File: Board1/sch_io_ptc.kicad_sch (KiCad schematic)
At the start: 5 parts, among them J2 PTC Plate, Q1 2N7002E, U4 AQG22205

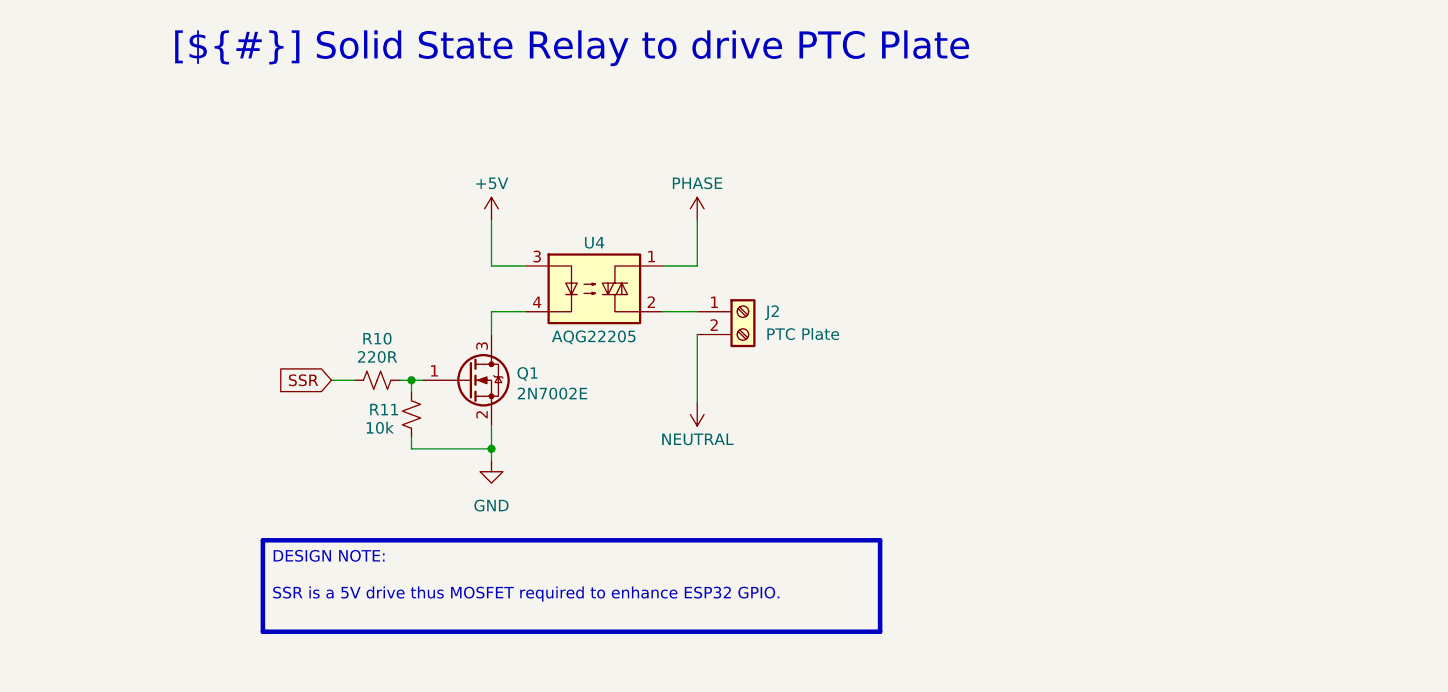
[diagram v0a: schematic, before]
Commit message: Resolve library and ERC issues
No changes to design.
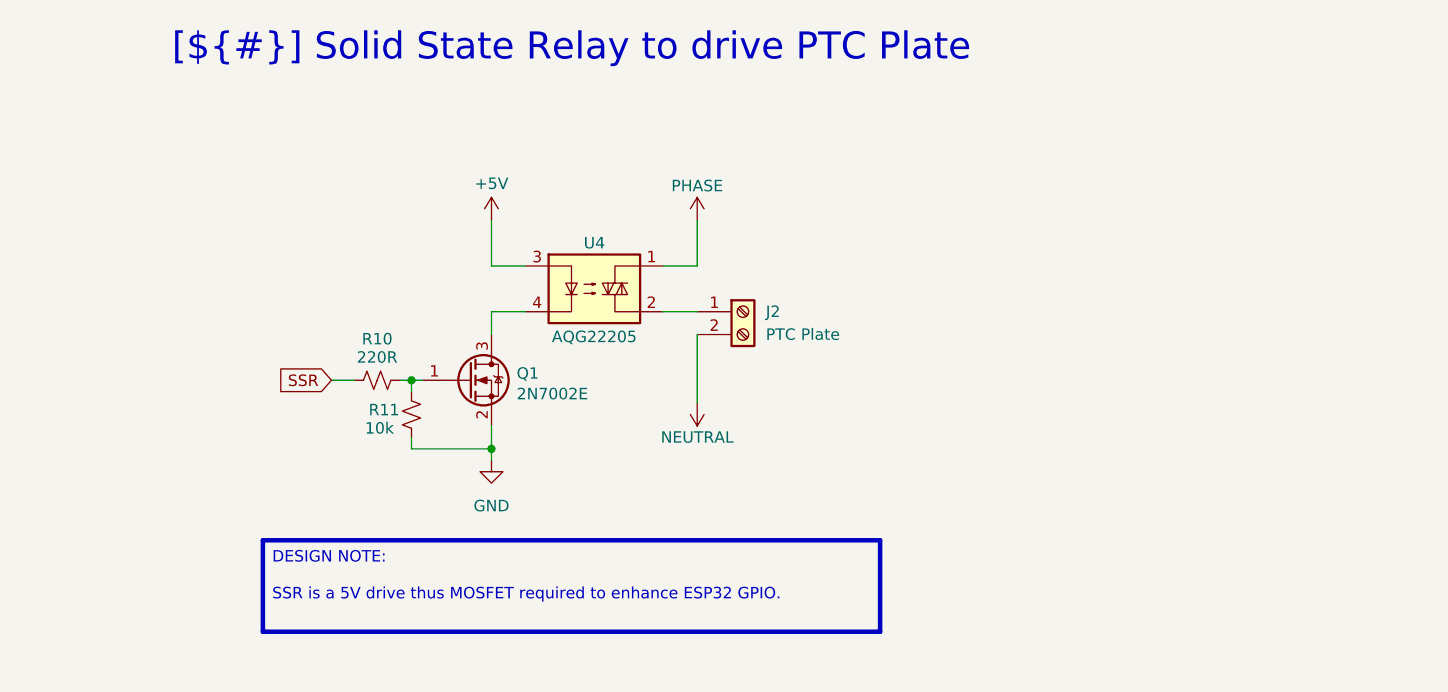
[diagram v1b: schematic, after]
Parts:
- U4: footprint Relay_THT:SSR_AQG22105 -> 0_Project:SSR_AQG22105
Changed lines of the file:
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@@
+	)
+	(symbol
+		(lib_id "power:LINE")
+		(at 162.56 38.1 0)
+		(unit 1)
+		(exclude_from_sim no)
+		(in_bom yes)
+		(on_board yes)
+		(dnp no)
+		(property "Reference" "#PWR601"
+			(at 162.56 41.91 0)
+			(effects
+				(font
+					(size 1.27 1.27)
+				)
+				(hide yes)
+			)
+		)
+		(property "Value" "PHASE"
+			(at 162.56 34.29 0)
+			(effects
+				(font
+					(size 1.27 1.27)
+				)
+			)
+		)
+		(property "Footprint" ""
+			(at 162.56 38.1 0)
+			(effects
+				(font
+					(size 1.27 1.27)
+				)
+				(hide yes)
+			)
+		)
+		(property "Datasheet" ""
+			(at 162.56 38.1 0)
+			(effects
+				(font
+					(size 1.27 1.27)
+				)
+				(hide yes)
+			)
+		)
+		(property "Description" "Power symbol creates a global label with name \"LINE\""
+			(at 162.56 38.1 0)
+			(effects
+				(font
+					(size 1.27 1.27)
+				)
+				(hide yes)
+			)
+		)
+		(property "Supplier" ""
+			(at 162.56 38.1 0)
+			(effects
+				(font
+					(size 1.27 1.27)
+				)
+				(hide yes)
+			)
+		)
+		(property "Digikey_PN" ""
+			(at 162.56 38.1 0)
+			(effects
+				(font
+					(size 1.27 1.27)
+				)
+				(hide yes)
+			)
+		)
+		(pin "1"
+		)
+		(instances
+			(project "Board1"
+				(path "/025ade93-30a9-4247-8f8c-ea2eaab4b489/9e03ffcc-3b99-446e-9ddf-2d137a044aaa"
+					(reference "#PWR601")
+					(unit 1)
+				)
+			)
+		)
 	)
 	(symbol
@@
 				(path "/025ade93-30a9-4247-8f8c-ea2eaab4b489/9e03ffcc-3b99-446e-9ddf-2d137a044aaa"
 					(reference "#PWR05")
-					(unit 1)
-				)
-			)
-		)
-	)
-	(symbol
-		(lib_id "power:LINE")
-		(at 162.56 58.42 180)
-		(unit 1)
-		(exclude_from_sim no)
-		(in_bom yes)
-		(on_board yes)
-		(dnp no)
-		(property "Reference" "#PWR024"
-			(at 162.56 54.61 0)
-			(effects
-				(font
-					(size 1.27 1.27)
-				)
-				(hide yes)
-			)
-		)
-		(property "Value" "NEUTRAL"
-			(at 162.56 62.484 0)
-			(effects
-				(font
-					(size 1.27 1.27)
-				)
-			)
-		)
-		(property "Footprint" ""
-			(at 162.56 58.42 0)
-			(effects
-				(font
-					(size 1.27 1.27)
-				)
-				(hide yes)
-			)
-		)
-		(property "Datasheet" ""
-			(at 162.56 58.42 0)
-			(effects
-				(font
-					(size 1.27 1.27)
-				)
-				(hide yes)
-			)
-		)
-		(property "Description" "Power symbol creates a global label with name \"LINE\""
-			(at 162.56 58.42 0)
-			(effects
-				(font
-					(size 1.27 1.27)
-				)
-				(hide yes)
-			)
-		)
-		(pin "1"
-		)
-		(instances
-			(project "Board1"
-				(path "/025ade93-30a9-4247-8f8c-ea2eaab4b489/9e03ffcc-3b99-446e-9ddf-2d137a044aaa"
-					(reference "#PWR024")
 					(unit 1)
 				)
@@
 	)
 	(symbol
-		(lib_id "power:LINE")
-		(at 162.56 38.1 0)
-		(unit 1)
-		(exclude_from_sim no)
-		(in_bom yes)
-		(on_board yes)
-		(dnp no)
-		(property "Reference" "#PWR020"
-			(at 162.56 41.91 0)
-			(effects
-				(font
-					(size 1.27 1.27)
-				)
-				(hide yes)
-			)
-		)
-		(property "Value" "PHASE"
-			(at 162.56 34.036 0)
-			(effects
-				(font
-					(size 1.27 1.27)
-				)
-			)
-		)
-		(property "Footprint" ""
-			(at 162.56 38.1 0)
-			(effects
-				(font
-					(size 1.27 1.27)
-				)
-				(hide yes)
-			)
-		)
-		(property "Datasheet" ""
-			(at 162.56 38.1 0)
-			(effects
-				(font
-					(size 1.27 1.27)
-				)
-				(hide yes)
-			)
-		)
-		(property "Description" "Power symbol creates a global label with name \"LINE\""
-			(at 162.56 38.1 0)
-			(effects
-				(font
-					(size 1.27 1.27)
-				)
-				(hide yes)
-			)
-		)
-		(pin "1"
-		)
-		(instances
-			(project "Board1"
-				(path "/025ade93-30a9-4247-8f8c-ea2eaab4b489/9e03ffcc-3b99-446e-9ddf-2d137a044aaa"
-					(reference "#PWR020")
-					(unit 1)
-				)
-			)
-		)
-	)
-	(symbol
 		(lib_id "Transistor_FET:2N7002E")
 		(at 137.16 55.88 0)
@@
 			)
 		)
-		(property "Footprint" "Relay_THT:SSR_AQG22105"
+		(property "Footprint" "0_Project:SSR_AQG22105"
 			(at 146.05 50.8 0)
 			(effects
@@
 					(unit 1)
 				)
+			)
+		)
+	)
+	(symbol
+		(lib_id "power:NEUT")
+		(at 162.56 58.42 180)
+		(unit 1)
+		(exclude_from_sim no)
+		(in_bom yes)
+		(on_board yes)
+		(dnp no)
+		(property "Reference" "#PWR602"
+			(at 162.56 54.61 0)
+			(effects
+				(font
+					(size 1.27 1.27)
+				)
+				(hide yes)
+			)
+		)
+		(property "Value" "NEUTRAL"
+			(at 162.56 62.23 0)
+			(effects
+				(font
+					(size 1.27 1.27)
+				)
+			)
+		)
+		(property "Footprint" ""
+			(at 162.56 58.42 0)
+			(effects
+				(font
+					(size 1.27 1.27)
+				)
+				(hide yes)
+			)
+		)
+		(property "Datasheet" ""
+			(at 162.56 58.42 0)
+			(effects
+				(font
+					(size 1.27 1.27)
+				)
+				(hide yes)
+			)
+		)
+		(property "Description" "Power symbol creates a global label with name \"NEUT\""
+			(at 162.56 58.42 0)
+			(effects
+				(font
+					(size 1.27 1.27)
+				)
+				(hide yes)
+			)
+		)
+		(property "Supplier" ""
+			(at 162.56 58.42 0)
+			(effects
+				(font
+					(size 1.27 1.27)
+				)
+				(hide yes)
+			)
+		)
+		(property "Digikey_PN" ""
+			(at 162.56 58.42 0)
+			(effects
+				(font
+					(size 1.27 1.27)
+				)
+				(hide yes)
+			)
+		)
+		(pin "1"
+		)
+		(instances
+			(project "Board1"
+				(path "/025ade93-30a9-4247-8f8c-ea2eaab4b489/9e03ffcc-3b99-446e-9ddf-2d137a044aaa"
+					(reference "#PWR602")
+					(unit 1)
+				)

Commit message: v1.2 release of board with bug fixes etc
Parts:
- removed J2: PTC Plate, TerminalBlock_Altech:Altech_AK100_1x02_P5.00mm, symbol Connector:Screw_Terminal_01x02
- added J2: PTC Plate, TerminalBlock_Altech:Altech_AK100_1x03_P5.00mm, symbol Connector:Screw_Terminal_01x03
- U4: value AQG22205 -> AQG22105; Digikey_PN 255-3752-ND -> 255-2102-5-ND; Supplier https://www.digikey.co.nz/en/products/detail/panasonic-electric-works/AQG22205/646006?s=N4IgTCBcDaIIIEUDiZUAYCsIC6BfIA -> https://www.digikey.co.nz/en/products/detail/panasonic-electric-works/AQG22105/646003?s=N4IgTCBcDaIIIEUDiYwEYAMBWEBdAvkA
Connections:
- net NEUTRAL: now also J2.3 (Pin_3)
- net at U4.2: now also J2.1 (Pin_1)
- no-connect marks 0 -> 1
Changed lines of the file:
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@@
 (kicad_sch
-	(version 20231120)
+	(version 20250114)
 	(generator "eeschema")
-	(generator_version "8.0")
+	(generator_version "9.0")
 	(paper "A4")
 	(title_block
 		(title "Solid State Relay to drive PTC Plate")
-		(date "2025-02-19")
-		(rev "1.1")
+		(date "2025-03-08")
+		(rev "1.2")
 		(company "Wattle Labs")
+	)
+	(text_box "DESIGN NOTE:\n\n1. SSR is a 5V drive thus MOSFET required to be driven by ESP32 GPIO\n2. SSR is a zero crossing type, best suited for the resistive load the PTC plate presents."
+		(exclude_from_sim no)
+		(at 114.3 74.93 0)
+		(size 78.74 13.335)
+		(margins 1.2025 1.2025 1.2025 1.2025)
+		(stroke
+			(width 0.5)
+			(type solid)
+			(color 200 200 200 1)
+		)
+		(fill
+			(type none)
+		)
+		(effects
+			(font
+				(size 1.27 1.27)
+				(color 0 0 0 1)
+			)
+			(justify left top)
+		)
+	)
+	(text_box "[${#}] ${TITLE}"
+		(exclude_from_sim no)
+		(at 12.065 12.065 0)
+		(size 273.05 13.335)
+		(margins 2.2499 2.2499 2.2499 2.2499)
+		(stroke
+			(width -0.0001)
+			(type default)
+		)
+		(fill
+			(type none)
+		)
+		(effects
+			(font
+				(size 3 3)
+				(thickness 0.375)
+			)
+		)
+	)
+	(text_box "DESIGN NOTE:\n\nSkipped pin 2 on J2 is intended to provide additional trace clearance VS finding a larger part (copper has been removed from PCB holes)."
+		(exclude_from_sim no)
+		(at 187.325 45.085 0)
+		(size 48.26 15.24)
+		(margins 1.2025 1.2025 1.2025 1.2025)
+		(stroke
+			(width 0.5)
+			(type solid)
+			(color 255 0 0 1)
+		)
+		(fill
+			(type none)
+		)
+		(effects
+			(font
+				(size 1.27 1.27)
+				(thickness 0.1588)
+				(color 255 0 0 1)
+			)
+			(justify left top)
+		)
 	)
 	(junction
@@
 		(color 0 0 0 0)
 	)
+	(no_connect
+		(at 162.56 50.8)
+	)
 	(wire
 		(pts
@@
 	(wire
 		(pts
-			(xy 162.56 50.8) (xy 162.56 58.42)
-		)
-		(stroke
-			(width 0)
-			(type default)
-		)
-	)
-	(wire
-		(pts
 			(xy 130.81 62.23) (xy 130.81 63.5)
 		)
@@
 		)
 	)
-	(text_box "DESIGN NOTE:\n\nSSR is a 5V drive thus MOSFET required to enhance ESP32 GPIO."
-		(exclude_from_sim no)
-		(at 114.3 73.66 0)
-		(size 68.58 10.16)
-		(stroke
-			(width 0.5)
-			(type solid)
-			(color 200 200 200 1)
-		)
-		(fill
-			(type none)
-		)
-		(effects
-			(font
-				(size 1.27 1.27)
-				(color 0 0 0 1)
-			)
-			(justify left top)
-		)
-	)
-	(text_box "[${#}] ${TITLE}"
-		(exclude_from_sim no)
-		(at 12.065 12.065 0)
-		(size 273.05 13.335)
-		(stroke
-			(width -0.0001)
-			(type default)
-		)
-		(fill
-			(type none)
-		)
-		(effects
-			(font
-				(size 3 3)
-				(thickness 0.375)
-			)
+	(wire
+		(pts
+			(xy 162.56 53.34) (xy 162.56 58.42)
+		)
+		(stroke
+			(width 0)
+			(type default)
 		)
 	)
@@
 	)
 	(symbol
+		(lib_id "Connector:Screw_Terminal_01x03")
+		(at 167.64 50.8 0)
+		(unit 1)
+		(exclude_from_sim no)
+		(in_bom yes)
+		(on_board yes)
+		(dnp no)
+		(fields_autoplaced yes)
+		(property "Reference" "J2"
+			(at 170.18 49.5299 0)
+			(effects
+				(font
+					(size 1.27 1.27)
+				)
+				(justify left)
+			)
+		)
+		(property "Value" "PTC Plate"
+			(at 170.18 52.0699 0)
+			(effects
+				(font
+					(size 1.27 1.27)
+				)
+				(justify left)
+			)
+		)
+		(property "Footprint" "TerminalBlock_Altech:Altech_AK100_1x03_P5.00mm"
+			(at 167.64 50.8 0)
+			(effects
+				(font
+					(size 1.27 1.27)
+				)
+				(hide yes)
+			)
+		)
+		(property "Datasheet" "~"
+			(at 167.64 50.8 0)
+			(effects
+				(font
+					(size 1.27 1.27)
+				)
+				(hide yes)
+			)
+		)
+		(property "Description" "Generic screw terminal, single row, 01x03, script generated (kicad-library-utils/schlib/autogen/connector/)"
+			(at 167.64 50.8 0)
+			(effects
+				(font
+					(size 1.27 1.27)
+				)
+				(hide yes)
+			)
+		)
+		(property "Supplier" ""
+			(at 167.64 50.8 0)
+			(effects
+				(font
+					(size 1.27 1.27)
+				)
+				(hide yes)
+			)
+		)
+		(property "Digikey_PN" ""
+			(at 167.64 50.8 0)
+			(effects
+				(font
+					(size 1.27 1.27)
+				)
+				(hide yes)
+			)
+		)
+		(pin "3"
+		)
+		(pin "1"
+		)
+		(pin "2"
+		)
+		(instances
+			(project ""
+				(path "/025ade93-30a9-4247-8f8c-ea2eaab4b489/9e03ffcc-3b99-446e-9ddf-2d137a044aaa"
+					(reference "J2")
+					(unit 1)
+				)
+			)
+		)
+	)
+	(symbol
 		(lib_id "Device:R_Small_US")
 		(at 130.81 59.69 0)
@@
 	)
 	(symbol
-		(lib_id "Connector:Screw_Terminal_01x02")
-		(at 167.64 48.26 0)
-		(unit 1)
-		(exclude_from_sim no)
-		(in_bom yes)
-		(on_board yes)
-		(dnp no)
-		(fields_autoplaced yes)
-		(property "Reference" "J2"
-			(at 170.18 48.2599 0)
-			(effects
-				(font
-					(size 1.27 1.27)
-				)
-				(justify left)
-			)
-		)
-		(property "Value" "PTC Plate"
-			(at 170.18 50.7999 0)
-			(effects
-				(font
-					(size 1.27 1.27)
-				)
-				(justify left)
-			)
-		)
-		(property "Footprint" "TerminalBlock_Altech:Altech_AK100_1x02_P5.00mm"
-			(at 167.64 48.26 0)
-			(effects
-				(font
-					(size 1.27 1.27)
-				)
-				(hide yes)
-			)
-		)
-		(property "Datasheet" "~"
-			(at 167.64 48.26 0)
-			(effects
-				(font
-					(size 1.27 1.27)
-				)
-				(hide yes)
-			)
-		)
-		(property "Description" "Generic screw terminal, single row, 01x02, script generated (kicad-library-utils/schlib/autogen/connector/)"
-			(at 167.64 48.26 0)
-			(effects
-				(font
-					(size 1.27 1.27)
-				)
-				(hide yes)
-			)
-		)
-		(property "Supplier" ""
-			(at 167.64 48.26 0)
-			(effects
-				(font
-					(size 1.27 1.27)
-				)
-				(hide yes)
-			)
-		)
-		(property "Digikey_PN" ""
-			(at 167.64 48.26 0)
-			(effects
-				(font
-					(size 1.27 1.27)
-				)
-				(hide yes)
-			)
-		)
-		(pin "1"
-		)
-		(pin "2"
-		)
-		(instances
-			(project "Board1"
-				(path "/025ade93-30a9-4247-8f8c-ea2eaab4b489/9e03ffcc-3b99-446e-9ddf-2d137a044aaa"
-					(reference "J2")
-					(unit 1)
-				)
-			)
-		)
-	)
-	(symbol
 		(lib_id "Device:R_Small_US")
 		(at 127 55.88 270)
@@
 			)
 		)
-		(property "Value" "AQG22205"
+		(property "Value" "AQG22105"
 			(at 151.13 51.054 0)
 			(effects
@@
 			)
 		)
-		(property "Description" "SSR RELAY SPST-NO 2A 75-264V"
+		(property "Description" "SSR RELAY SPST-NO 2A 75-264VAC Zero Cross"
 			(at 151.13 45.72 0)
 			(effects
@@
 			)
 		)
-		(property "Supplier" "https://www.digikey.co.nz/en/products/detail/panasonic-electric-works/AQG22205/646006?s=N4IgTCBcDaIIIEUDiZUAYCsIC6BfIA"
+		(property "Supplier" "https://www.digikey.co.nz/en/products/detail/panasonic-electric-works/AQG22105/646003?s=N4IgTCBcDaIIIEUDiYwEYAMBWEBdAvkA"
 			(at 151.13 45.72 0)
 			(effects
@@
 			)
 		)
-		(property "Digikey_PN" "255-3752-ND"
+		(property "Digikey_PN" "255-2102-5-ND"
 			(at 151.13 45.72 0)
 			(effects
